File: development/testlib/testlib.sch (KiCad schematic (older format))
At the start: 1 part

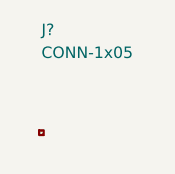
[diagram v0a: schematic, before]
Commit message: Figured out field names! Wickerlib is done except for symbols.
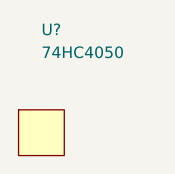
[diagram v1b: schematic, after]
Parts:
- removed J?: CONN-1x05, CONN-1x05-2.54MM-TH, symbol CONN-1x05
- added U?: 74HC4050, SOIC16, symbol 74HC4050
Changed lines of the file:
@@
 $EndDescr
 $Comp
-L CONN-1x05 J?
-U 1 1 5711D699
+L 74HC4050 U?
+U 1 1 57181D7B
 P 4475 3525
-F 0 "J?" H 4475 3975 50  0000 L CNN
-F 1 "CONN-1x05" H 4475 3875 50  0000 L CNN
-F 2 "CONN-1x05-2.54MM-TH" H 4475 3175 50  0001 C CIN
-F 3 "https://cdn.harwin.com/pdfs/60page140.pdf" H 4475 3525 50  0001 C CIN
+F 0 "U?" H 4475 3975 50  0000 L CNN
+F 1 "74HC4050" H 4475 3875 50  0000 L CNN
+F 2 "SOIC16" H 4475 3175 50  0001 C CIN
+F 3 "http://www.nxp.com/documents/data_sheet/74HC4050.pdf" H 4475 3525 5   0001 C CNN
+F 4 "SOIC16" H 4475 3175 50  0001 C CIN "Field4"
+F 5 "NXP" H 4475 3175 50  0001 C CIN "Field5"
+F 6 "Not Verified" H 4475 3175 50  0001 C CIN "Field6"
+F 7 "Digikey" H 4475 3175 50  0001 C CIN "Field7"
+F 8 "568-1453-5-ND" H 4475 3175 50  0001 C CIN "Field8"
 	1    4475 3525
 	1    0    0    -1

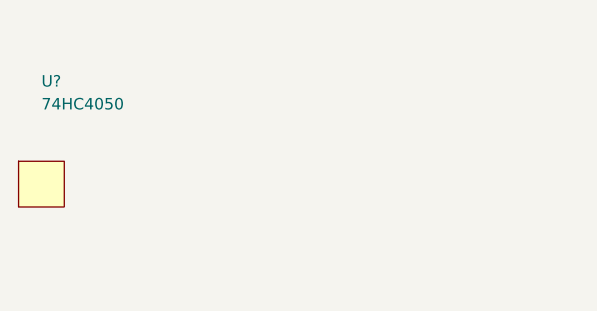
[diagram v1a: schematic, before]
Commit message: Changing how the names and values are set up in inventory to make wickerlib generation easier.
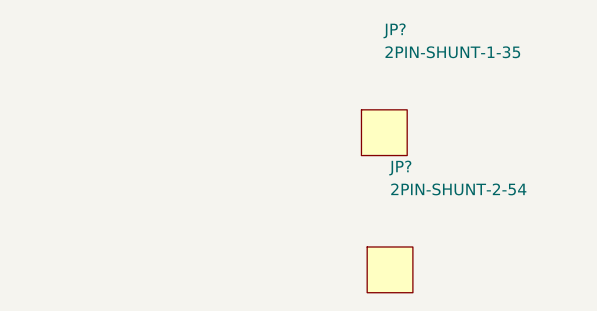
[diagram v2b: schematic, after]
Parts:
- removed U?: 74HC4050, SOIC16, symbol 74HC4050
- added JP?: 2PIN-SHUNT-1-35, CONN-1x02-2.54MM-TH, symbol 2PIN-SHUNT-1-35
- added JP?: 2PIN-SHUNT-2-54, CONN-1x02-2.54MM-TH, symbol 2PIN-SHUNT-2-54
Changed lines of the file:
@@
 EESchema Schematic File Version 2
 LIBS:wickerlib
+LIBS:xilinx
+LIBS:video
+LIBS:valves
+LIBS:ttl_ieee
+LIBS:transf
+LIBS:texas
+LIBS:switches
+LIBS:supertex
+LIBS:stm8
+LIBS:stm32
+LIBS:siliconi
+LIBS:silabs
+LIBS:sensors
+LIBS:rfcom
+LIBS:relays
+LIBS:references
+LIBS:pspice
+LIBS:powerint
+LIBS:power
+LIBS:philips
+LIBS:opto
+LIBS:onsemi
+LIBS:nxp_armmcu
+LIBS:nordicsemi
+LIBS:msp430
+LIBS:motorola
+LIBS:motor_drivers
+LIBS:microcontrollers
+LIBS:microchip_pic32mcu
+LIBS:microchip_pic18mcu
+LIBS:microchip_pic16mcu
+LIBS:microchip_pic12mcu
+LIBS:microchip_pic10mcu
+LIBS:microchip_dspic33dsc
+LIBS:microchip
+LIBS:memory
+LIBS:maxim
+LIBS:logo
+LIBS:linear
+LIBS:ir
+LIBS:intel
+LIBS:hc11
+LIBS:graphic
+LIBS:gennum
+LIBS:ftdi
+LIBS:elec-unifil
+LIBS:dsp
+LIBS:display
+LIBS:diode
+LIBS:digital-audio
+LIBS:device
+LIBS:dc-dc
+LIBS:cypress
+LIBS:contrib
+LIBS:conn
+LIBS:cmos_ieee
+LIBS:cmos4000
+LIBS:brooktre
+LIBS:audio
+LIBS:analog_switches
+LIBS:analog_devices
+LIBS:adc-dac
+LIBS:actel
+LIBS:ac-dc
+LIBS:Zilog
+LIBS:Xicor
+LIBS:Power_Management
+LIBS:Oscillators
+LIBS:Lattice
+LIBS:ESD_Protection
+LIBS:Altera
+LIBS:74xgxx
+LIBS:interface
+LIBS:regul
+LIBS:atmel
+LIBS:74xx
+LIBS:transistors
 LIBS:testlib-cache
 EELAYER 25 0
@@
 $EndDescr
 $Comp
-L 74HC4050 U?
-U 1 1 57181D7B
-P 4475 3525
-F 0 "U?" H 4475 3975 50  0000 L CNN
-F 1 "74HC4050" H 4475 3875 50  0000 L CNN
-F 2 "SOIC16" H 4475 3175 50  0001 C CIN
-F 3 "http://www.nxp.com/documents/data_sheet/74HC4050.pdf" H 4475 3525 5   0001 C CNN
-F 4 "SOIC16" H 4475 3175 50  0001 C CIN "Field4"
-F 5 "NXP" H 4475 3175 50  0001 C CIN "Field5"
-F 6 "Not Verified" H 4475 3175 50  0001 C CIN "Field6"
-F 7 "Digikey" H 4475 3175 50  0001 C CIN "Field7"
-F 8 "568-1453-5-ND" H 4475 3175 50  0001 C CIN "Field8"
-	1    4475 3525
+L 2PIN-SHUNT-1-35 JP?
+U 1 1 571835B2
+P 5975 3300
+F 0 "JP?" H 5975 3750 50  0000 L CNN
+F 1 "2PIN-SHUNT-1-35" H 5975 3650 50  0000 L CNN
+F 2 "CONN-1x02-2.54MM-TH" H 5975 2950 50  0001 C CIN
+F 3 "http://multimedia.3m.com/mws/mediawebserver?66666UuZjcFSLXTtNxTElXf6EVuQEcuZgVs6EVs6E666666--" H 5975 3300 5   0001 C CNN
+F 4 "CONN-1x02-2.54MM-TH" H 5975 2950 50  0001 C CIN "Package"
+F 5 "3M" H 5975 2950 50  0001 C CIN "MF_Name"
+F 6 "969102-0000-DA" H 5975 2950 50  0001 C CIN "MF_PN"
+F 7 "Digikey" H 5975 2950 50  0001 C CIN "S1_Name"
+F 8 "3M9580-ND" H 5975 2950 50  0001 C CIN "S1_PN"
+F 9 "SHUNT JUMPER 0.1IN BLACK GOLD" H 5975 2950 50  0001 C CIN "Description"
+F 10 "Not Verified" H 5975 2950 50  0001 C CIN "Verified"
+	1    5975 3300
 	1    0    0    -1
 $EndComp
+$Comp
+L 2PIN-SHUNT-2-54 JP?
+U 1 1 571835F6
+P 6000 3900
+F 0 "JP?" H 6000 4350 50  0000 L CNN
+F 1 "2PIN-SHUNT-2-54" H 6000 4250 50  0000 L CNN
+F 2 "CONN-1x02-2.54MM-TH" H 6000 3550 50  0001 C CIN
+F 3 "http://multimedia.3m.com/mws/mediawebserver?66666UuZjcFSLXTtNxTElXf6EVuQEcuZgVs6EVs6E666666--" H 6000 3900 5   0001 C CNN
+F 4 "CONN-1x02-2.54MM-TH" H 6000 3550 50  0001 C CIN "Package"
+F 5 "3M" H 6000 3550 50  0001 C CIN "MF_Name"
+F 6 "969102-0000-DA" H 6000 3550 50  0001 C CIN "MF_PN"
+F 7 "Digikey" H 6000 3550 50  0001 C CIN "S1_Name"
+F 8 "3M9580-ND" H 6000 3550 50  0001 C CIN "S1_PN"
+F 9 "SHUNT JUMPER 0.1IN BLACK GOLD" H 6000 3550 50  0001 C CIN "Description"
+F 10 "Not Verified" H 6000 3550 50  0001 C CIN "Verified"
+	1    6000 3900
+	1    0    0    -1
+$EndComp
